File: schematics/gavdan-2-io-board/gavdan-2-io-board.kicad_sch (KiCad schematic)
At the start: 23 parts

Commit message: Updates to schematics to correct errors
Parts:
- removed U? (x4): 74LS08, symbol 74xx:74LS08
- removed U? (x4): 74LS04, symbol 74xx:74LS04
- removed U?: 74LS133, symbol 74xx:74LS133
- added C2: 33pF, symbol Device:C
- added J1: DB9_Female, symbol Connector:DB9_Female
- added R1: R, symbol Device:R
- added U6: MAX233CPP, DIP794W47P254L2654H457Q20, symbol MAX233CPP_G36:MAX233CPP+G36
- added Y1: 1.8432MHZ, symbol Device:Crystal
- gave numbers to parts that had none: 8
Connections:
- net +5V: now also U6.7 (VCC)
- net GND: now also U5.16 (~{DCD}), U5.17 (~{DSR}), U5.9 (~{CTS}), U7.23 (~{CS2}), C2.2, U6.6 (GND), U6.9 (GND)
- net at U5.10 (TxD): now also U6.2 (T1IN)
- net at U5.12 (RxD): now also U6.3 (R1OUT)
- net at U5.6 (XTAL1): now also C2.1, R1.1, Y1.2
- net at U5.7 (XTAL2): now also R1.2, Y1.1
- net PA0: now reaches U7.2 (PA0)
- net PA0: now also U7.3 (PA1), U7.4 (PA2), U7.5 (PA3), U7.6 (PA4), U7.7 (PA5), U7.8 (PA6), U7.9 (PA7)
- net at U7.24 (CS1): now also U4.8
- new net: U6.10 (C2-), U6.16 (C2-)
- new net: U6.11 (C2+), U6.15 (C2+)
- new net: J1.2, U6.4 (R1IN)
- new net: J1.3, U6.5 (T1OUT)
- no-connect marks 1 -> 27
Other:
- note added: "Address lines from expansion bus"
- note added: "Circuit diagram for GAVDAN-2 Microcomputer"
- note added: "Control lines from expansion bus"
- note added: "Data lines from expansion bus"
- note added: "Reserved for expansion"
- note added: "User expansion port"
- note removed: "R/W"
- title: GAVDAN-2 Reset circuit, Clock, 6502 CPU, RAM and ROM -> GAVDAN-2 IO Board
- moved on the sheet: C1, C3, U1C, U1D, U1E, U2A, U3A, U3B, U3C, U3D, U4C, U4D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

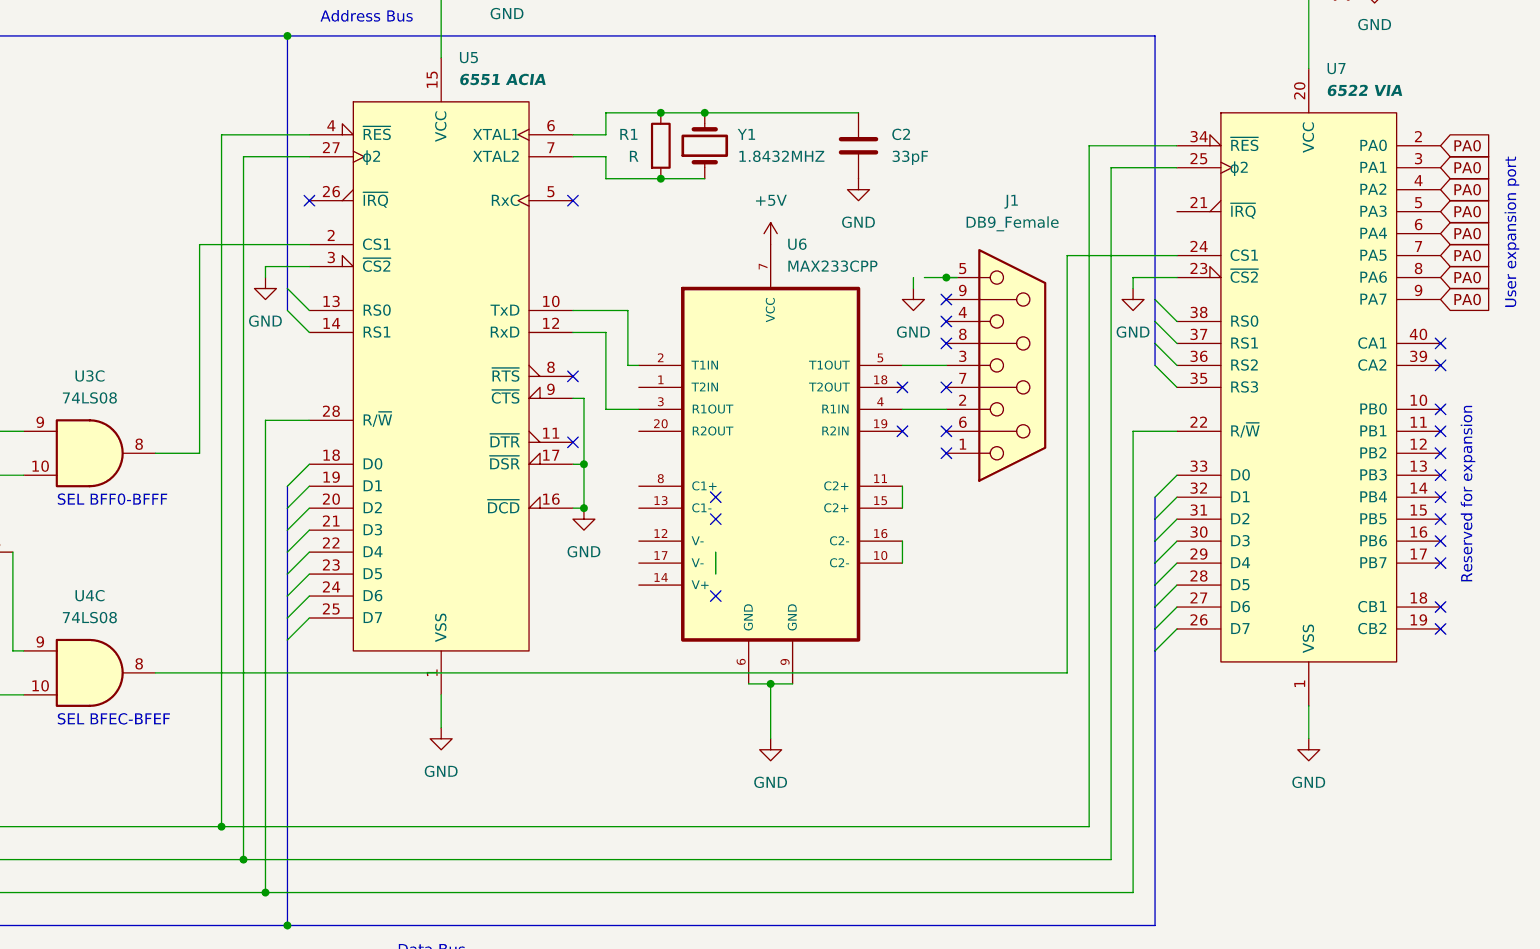
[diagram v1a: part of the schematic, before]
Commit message: Minor corrections to IO board schematic
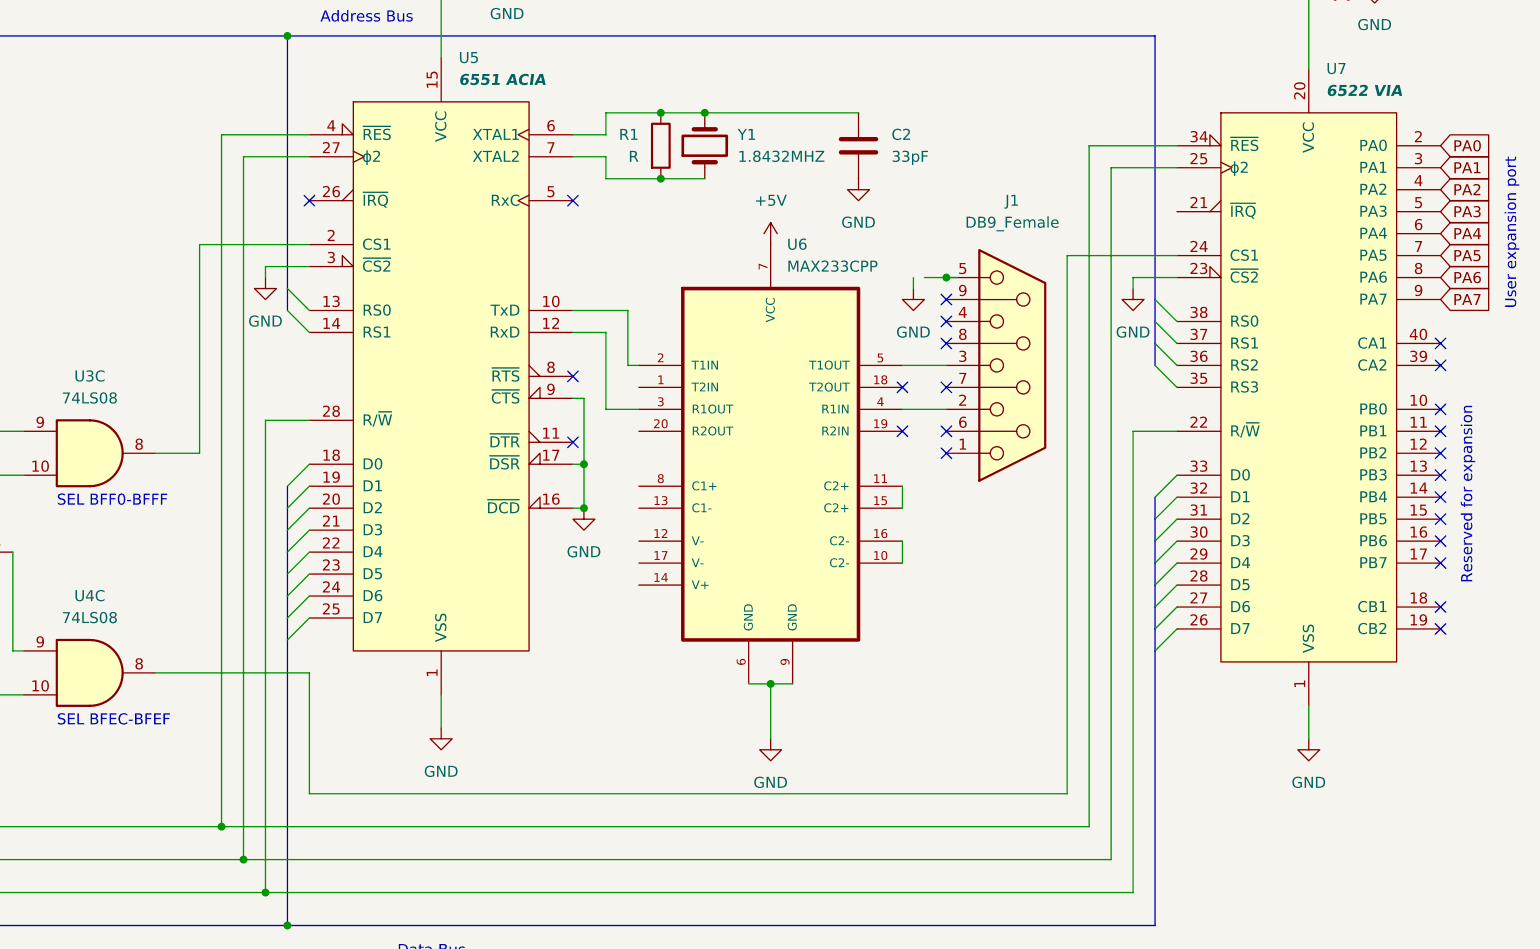
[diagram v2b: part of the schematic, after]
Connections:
- net PA0: no longer U7.3 (PA1), U7.4 (PA2), U7.5 (PA3), U7.6 (PA4), U7.7 (PA5), U7.8 (PA6), U7.9 (PA7)
- new net PA1: U7.3 (PA1)
- new net PA2: U7.4 (PA2)
- new net PA3: U7.5 (PA3)
- new net PA4: U7.6 (PA4)
- new net PA5: U7.7 (PA5)
- new net PA6: U7.8 (PA6)
- new net PA7: U7.9 (PA7)
- no-connect marks 27 -> 24
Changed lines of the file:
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@@
   (no_connect (at 165.1 76.2))
   (no_connect (at 165.1 55.88))
-  (no_connect (at 181.61 90.17))
-  (no_connect (at 181.61 92.71))
   (no_connect (at 208.28 85.09))
   (no_connect (at 208.28 72.39))
@@
   (no_connect (at 208.28 69.85))
   (no_connect (at 165.1 83.82))
-  (no_connect (at 181.61 101.6))
   (no_connect (at 203.2 77.47))
   (no_connect (at 203.2 82.55))
@@
     (stroke (width 0) (type default) (color 0 0 0 0))
   )
-  (wire (pts (xy 222.25 110.49) (xy 222.25 62.23))
+  (wire (pts (xy 222.25 62.23) (xy 222.25 124.46))
     (stroke (width 0) (type default) (color 0 0 0 0))
   )
@@
     (stroke (width 0) (type default) (color 0 0 0 0))
   )
+  (wire (pts (xy 134.62 110.49) (xy 134.62 124.46))
+    (stroke (width 0) (type default) (color 0 0 0 0))
+  )
   (bus (pts (xy 30.48 72.39) (xy 30.48 76.2))
     (stroke (width 0) (type default) (color 0 0 0 0))
   )
+  (wire (pts (xy 134.62 124.46) (xy 222.25 124.46))
+    (stroke (width 0) (type default) (color 0 0 0 0))
+  )
   (bus (pts (xy 132.08 36.83) (xy 132.08 66.04))
     (stroke (width 0) (type default) (color 0 0 0 0))
@@
     (stroke (width 0) (type default) (color 0 0 0 0))
   )
+  (wire (pts (xy 116.84 110.49) (xy 134.62 110.49))
+    (stroke (width 0) (type default) (color 0 0 0 0))
+  )
   (wire (pts (xy 58.42 80.01) (xy 58.42 77.47))
     (stroke (width 0) (type default) (color 0 0 0 0))
@@
     (stroke (width 0) (type default) (color 0 0 0 0))
   )
-  (wire (pts (xy 116.84 110.49) (xy 222.25 110.49))
-    (stroke (width 0) (type default) (color 0 0 0 0))
-  )
   (bus (pts (xy 30.48 64.77) (xy 30.48 68.58))
     (stroke (width 0) (type default) (color 0 0 0 0))
@@
   )
   (bus (pts (xy 41.91 39.37) (xy 41.91 46.99))
-    (stroke (width 0) (type default) (color 0 0 0 0))
-  )
-  (wire (pts (xy 181.61 96.52) (xy 181.61 99.06))
     (stroke (width 0) (type default) (color 0 0 0 0))
   )
@@
     )
   )
-  (global_label "PA0" (shape input) (at 265.43 59.69 0) (fields_autoplaced)
+  (global_label "PA4" (shape input) (at 265.43 59.69 0) (fields_autoplaced)
     (effects (font (size 1.27 1.27)) (justify left))
     (property "Intersheet References" "${INTERSHEET_REFS}" (id 0) (at 271.4112 59.6106 0)
@@
     )
   )
-  (global_label "PA0" (shape input) (at 265.43 64.77 0) (fields_autoplaced)
+  (global_label "PA6" (shape input) (at 265.43 64.77 0) (fields_autoplaced)
     (effects (font (size 1.27 1.27)) (justify left))
     (property "Intersheet References" "${INTERSHEET_REFS}" (id 0) (at 271.4112 64.6906 0)
@@
     )
   )
-  (global_label "PA0" (shape input) (at 265.43 54.61 0) (fields_autoplaced)
+  (global_label "PA2" (shape input) (at 265.43 54.61 0) (fields_autoplaced)
     (effects (font (size 1.27 1.27)) (justify left))
     (property "Intersheet References" "${INTERSHEET_REFS}" (id 0) (at 271.4112 54.5306 0)
@@
     )
   )
-  (global_label "PA0" (shape input) (at 265.43 52.07 0) (fields_autoplaced)
+  (global_label "PA1" (shape input) (at 265.43 52.07 0) (fields_autoplaced)
     (effects (font (size 1.27 1.27)) (justify left))
     (property "Intersheet References" "${INTERSHEET_REFS}" (id 0) (at 271.4112 51.9906 0)
@@
     )
   )
-  (global_label "PA0" (shape input) (at 265.43 57.15 0) (fields_autoplaced)
+  (global_label "PA3" (shape input) (at 265.43 57.15 0) (fields_autoplaced)
     (effects (font (size 1.27 1.27)) (justify left))
     (property "Intersheet References" "${INTERSHEET_REFS}" (id 0) (at 271.4112 57.0706 0)
@@
     )
   )
-  (global_label "PA0" (shape input) (at 265.43 67.31 0) (fields_autoplaced)
+  (global_label "PA7" (shape input) (at 265.43 67.31 0) (fields_autoplaced)
     (effects (font (size 1.27 1.27)) (justify left))
     (property "Intersheet References" "${INTERSHEET_REFS}" (id 0) (at 271.4112 67.2306 0)
@@
     )
   )
-  (global_label "PA0" (shape input) (at 265.43 62.23 0) (fields_autoplaced)
+  (global_label "PA5" (shape input) (at 265.43 62.23 0) (fields_autoplaced)
     (effects (font (size 1.27 1.27)) (justify left))
     (property "Intersheet References" "${INTERSHEET_REFS}" (id 0) (at 271.4112 62.1506 0)
